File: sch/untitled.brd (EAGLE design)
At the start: 50 x 50 mm, 25 parts, among them J1 AVR_SPI_PRG_62X3_LOCK, Q1 20MHz, U1 ATMEGA328P, X1 SM06B-SSR-H-TB

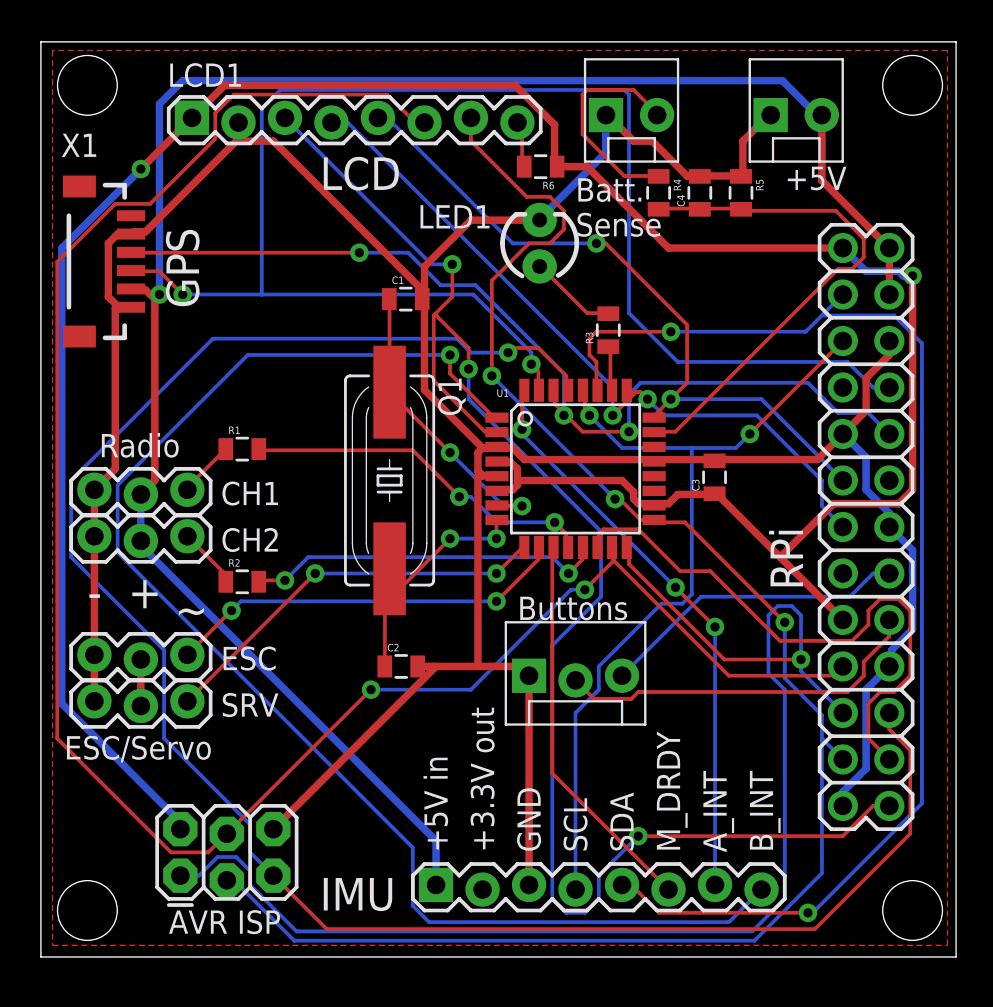
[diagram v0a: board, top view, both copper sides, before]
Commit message: Better PCB annotations, moved stuff and re-routed
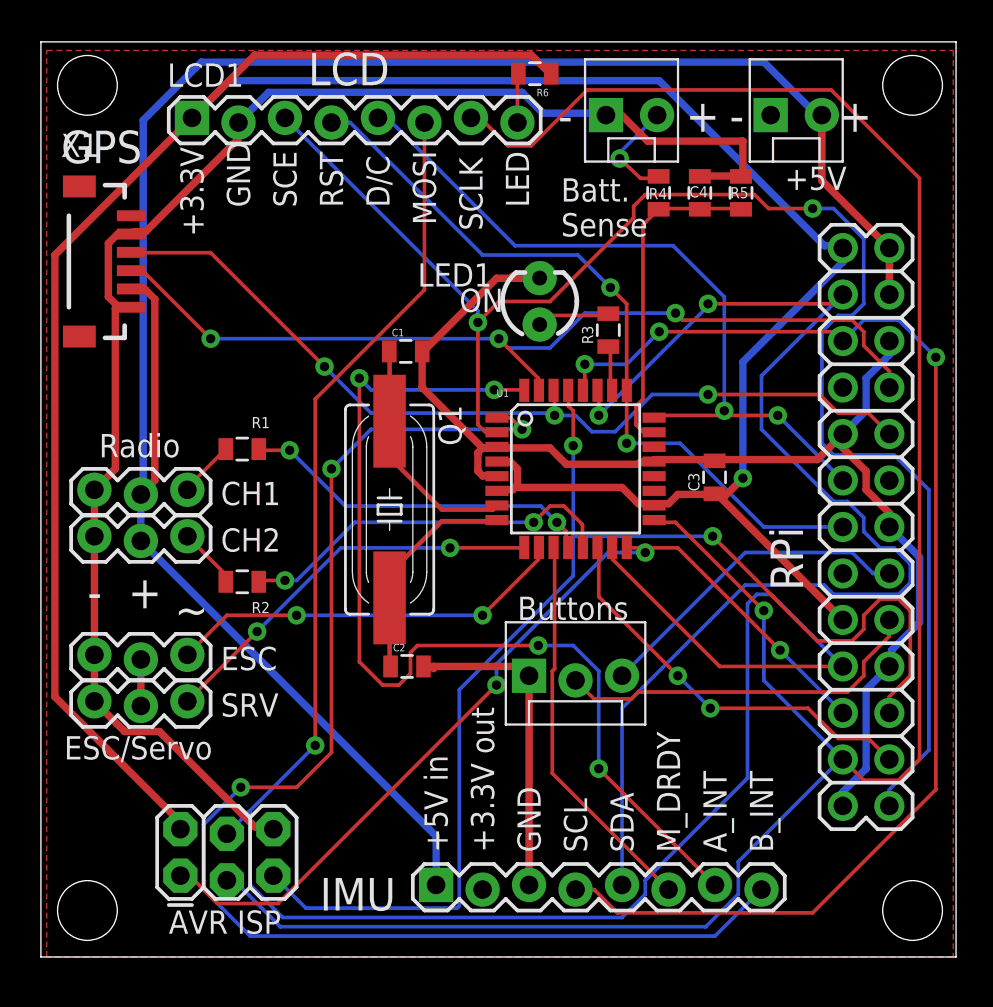
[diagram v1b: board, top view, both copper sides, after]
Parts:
- moved R6 5.09 mm to (27.0, 48.3)
- moved LED1 3.17 mm to (27.2, 35.8)
- moved C1 2.86 mm to (19.9, 33.1)
- moved Q1 1.59 mm to (19.1, 24.4)
- moved C2 0.32 mm to (20.0, 15.9)
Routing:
- net TXD0: track 84.6 -> 50.4 mm, vias 2 -> 3
- net AVR_RST: track 103.6 -> 70.3 mm, vias 1 -> 2
- net SCLK: track 92.4 -> 122.8 mm, vias 3 -> 1
- net SCL1: track 46.0 -> 69.6 mm, vias 2 -> 3
- net A_INT: track 31.4 -> 54.8 mm, vias 3 -> 4
- net MISO: track 73.2 -> 50.4 mm, vias 1 -> 3
- net GND: track 183.2 -> 169.1 mm
- net +3V3: track 135.7 -> 148.1 mm, vias 2 -> 1
- net +5V: track 100.1 -> 112.0 mm, vias 1 -> 0
- net N$12: track 28.4 -> 18.0 mm
- net SPI_CE0: track 32.1 -> 22.3 mm, vias 0 -> 2
- net N$11: track 12.1 -> 5.82 mm, vias 0 -> 1
- net MOSI: track 107.0 -> 111.1 mm, vias 2 -> 1
- net N$2: track 16.0 -> 12.2 mm, vias 2 -> 0
- net N$1: track 16.3 -> 12.9 mm, vias 2 -> 0
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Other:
- board text added: "+3.3V"
- board text added: "D/C"
- board text added: "LED"
- board text added: "MOSI"
- board text added: "ON"
- board text added: "RST"
- board text added: "SCE"
- board text added: "SCLK"

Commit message: critical PCB connector fixes
 - flipped RPi connector around to correct orientation
 - flipped SiRF GPS connector around
 - added two more resistors to radio input, so there's a resistor
   divider instead of relying on overload protection
 - powered LCD backlight LED by 5v instead of 3.3v, resistor can adjust
   brightness
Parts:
- added R7, R8: 10k, SparkFun-Resistors:0805
- moved JP1 32.2 mm to (46.4, 6.67), turned to 90 degrees
- moved X1 26.4 mm to (3.00, 11.6)
- moved R1 9.85 mm to (11.4, 37.6)
- moved R2 9.85 mm to (11.4, 30.3)
- moved CH1 9.85 mm to (3.24, 35.2)
- moved CH2 9.85 mm to (3.24, 32.7)
- moved ESC 9.85 mm to (3.24, 26.2)
- moved SRV 9.85 mm to (3.24, 23.7)
- moved J1 3.70 mm to (10.8, 6.35)
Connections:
- net N$7 renamed LCD_LED
- net +3V3: no longer R6.1
- net +5V: now also R6.1, X1.2; no longer X1.5
- net GND: now also R7.1, R8.1, X1.1, X1.5; no longer X1.2, X1.6
- net N$4: now also R7.2
- net N$5: now also R8.2
- net RXD0: now also X1.4; no longer X1.3
- net TXD0: now also X1.3; no longer X1.4
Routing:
- net N$4: track 19.6 -> 81.0 mm
- net MISO: track 50.4 -> 107.6 mm
- net GND: track 169.1 -> 221.9 mm
- net B_INT: track 73.2 -> 37.9 mm, vias 3 -> 1
- net RXD0: track 48.6 -> 82.7 mm, vias 3 -> 5
- net +3V3: track 148.1 -> 115.8 mm, vias 1 -> 3
- net SPI_CE1: track 85.3 -> 57.1 mm
- net +5V: track 112.0 -> 140.2 mm, vias 0 -> 1
- net GPIO24: track 20.3 -> 48.3 mm
- net MOSI: track 111.1 -> 85.1 mm, vias 1 -> 4
- net A_INT: track 54.8 -> 74.4 mm, vias 4 -> 2
- net AVR_RST: track 70.3 -> 87.8 mm, vias 2 -> 3
- net TXD0: track 50.4 -> 65.8 mm, vias 3 -> 4
- net LCD_RST: track 41.6 -> 55.6 mm
- net SCLK: track 122.8 -> 114.1 mm, vias 1 -> 2
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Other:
- board text added: "1"
- board text added: "2"
- board text added: "25"
- board text added: "26"
- board text added: "6"
- board text added: "RX"
- board text added: "TX"
